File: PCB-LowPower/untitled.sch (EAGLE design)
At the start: 23 parts, among them J1 RJ45-8N-B, J2 22-27-2041-04, U1 ESP32-DEVKITC-32D, X1 MSTBA2

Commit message: revisi PCB
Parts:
- added J3: 22-27-2051-05, con-molex:22-27-2051-05
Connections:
- net 3V3: now also J3-5.S
- net GND: now also J3-1.S
- net P2_1: now also J3-4.S; no longer U1.IO5
- net P2_2: now also J3-3.S; no longer U1.IO2
- net RST_Z: now also J3-2.S
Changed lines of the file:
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@@
 <part name="R6" library="adafruit" library_urn="urn:adsk.eagle:library:420" deviceset="R-US_" device="M0805" package3d_urn="urn:adsk.eagle:package:6240587/1"/>
 <part name="GND9" library="supply1" library_urn="urn:adsk.eagle:library:371" deviceset="GND" device=""/>
+<part name="J3" library="con-molex" library_urn="urn:adsk.eagle:library:165" deviceset="22-?-05" device="27-2051" package3d_urn="urn:adsk.eagle:package:8078651/1"/>
+<part name="GND10" library="supply1" library_urn="urn:adsk.eagle:library:371" deviceset="GND" device=""/>
 </parts>
 <sheets>
@@
 <attribute name="VALUE" x="27.94" y="-25.4" size="1.778" layer="96"/>
 </instance>
+<instance part="J3" gate="-1" x="-58.42" y="-38.1" smashed="yes" rot="R180">
+<attribute name="NAME" x="-60.96" y="-37.338" size="1.524" layer="95" rot="R180"/>
+<attribute name="VALUE" x="-57.658" y="-39.497" size="1.778" layer="96" rot="R180"/>
+</instance>
+<instance part="J3" gate="-2" x="-58.42" y="-33.02" smashed="yes" rot="R180">
+<attribute name="NAME" x="-60.96" y="-32.258" size="1.524" layer="95" rot="R180"/>
+</instance>
+<instance part="J3" gate="-3" x="-58.42" y="-27.94" smashed="yes" rot="R180">
+<attribute name="NAME" x="-60.96" y="-27.178" size="1.524" layer="95" rot="R180"/>
+</instance>
+<instance part="J3" gate="-4" x="-58.42" y="-22.86" smashed="yes" rot="R180">
+<attribute name="NAME" x="-60.96" y="-22.098" size="1.524" layer="95" rot="R180"/>
+</instance>
+<instance part="J3" gate="-5" x="-58.42" y="-17.78" smashed="yes" rot="R180">
+<attribute name="NAME" x="-60.96" y="-17.018" size="1.524" layer="95" rot="R180"/>
+</instance>
+<instance part="GND10" gate="1" x="-53.34" y="-43.18" smashed="yes">
+<attribute name="VALUE" x="-55.88" y="-45.72" size="1.778" layer="96"/>
+</instance>
 </instances>
 <busses>
@@
 <wire x1="50.8" y1="-2.54" x2="50.8" y2="0" width="0.1524" layer="91"/>
 <label x="50.8" y="0" size="0.6096" layer="95" rot="R90" xref="yes"/>
+</segment>
+<segment>
+<pinref part="J3" gate="-5" pin="S"/>
+<wire x1="-55.88" y1="-17.78" x2="-53.34" y2="-17.78" width="0.1524" layer="91"/>
+<label x="-53.34" y="-17.78" size="0.6096" layer="95" xref="yes"/>
 </segment>
 </net>
@@
 <junction x="35.56" y="-17.78"/>
 </segment>
+<segment>
+<pinref part="J3" gate="-1" pin="S"/>
+<wire x1="-55.88" y1="-38.1" x2="-53.34" y2="-38.1" width="0.1524" layer="91"/>
+<pinref part="GND10" gate="1" pin="GND"/>
+<wire x1="-53.34" y1="-38.1" x2="-53.34" y2="-40.64" width="0.1524" layer="91"/>
+</segment>
 </net>
 <net name="MOSI_HSPI" class="0">
@@
 <label x="53.34" y="-15.24" size="0.6096" layer="95" xref="yes"/>
 </segment>
+<segment>
+<pinref part="J3" gate="-2" pin="S"/>
+<wire x1="-55.88" y1="-33.02" x2="-53.34" y2="-33.02" width="0.1524" layer="91"/>
+<label x="-53.34" y="-33.02" size="0.6096" layer="95" xref="yes"/>
+</segment>
 </net>
 <net name="RX_Z" class="0">
@@
 <net name="P2_1" class="0">
 <segment>
-<pinref part="U1" gate="G$1" pin="IO5"/>
-<wire x1="-5.08" y1="48.26" x2="-2.54" y2="48.26" width="0.1524" layer="91"/>
-<label x="-2.54" y="48.26" size="0.6096" layer="95" xref="yes"/>
-</segment>
-<segment>
 <pinref part="U$1" gate="G$1" pin="P2.1"/>
 <wire x1="-43.18" y1="-7.62" x2="-45.72" y2="-7.62" width="0.1524" layer="91"/>
 <label x="-45.72" y="-7.62" size="0.6096" layer="95" rot="R180" xref="yes"/>
 </segment>
+<segment>
+<pinref part="J3" gate="-4" pin="S"/>
+<wire x1="-55.88" y1="-22.86" x2="-53.34" y2="-22.86" width="0.1524" layer="91"/>
+<label x="-53.34" y="-22.86" size="0.6096" layer="95" xref="yes"/>
+</segment>
 </net>
 <net name="P2_2" class="0">
-<segment>
-<pinref part="U1" gate="G$1" pin="IO2"/>
-<wire x1="-5.08" y1="35.56" x2="-2.54" y2="35.56" width="0.1524" layer="91"/>
-<label x="-2.54" y="35.56" size="0.6096" layer="95" xref="yes"/>
-</segment>
 <segment>
 <pinref part="U$1" gate="G$1" pin="P2.2"/>
@@
 <label x="-45.72" y="-5.08" size="0.6096" layer="95" rot="R180" xref="yes"/>
 </segment>
-</net>
+<segment>
+<pinref part="J3" gate="-3" pin="S"/>
+<wire x1="-55.88" y1="-27.94" x2="-53.34" y2="-27.94" width="0.1524" layer="91"/>
+<label x="-53.34" y="-27.94" size="0.6096" layer="95" xref="yes"/>
+</segment>
+</net>

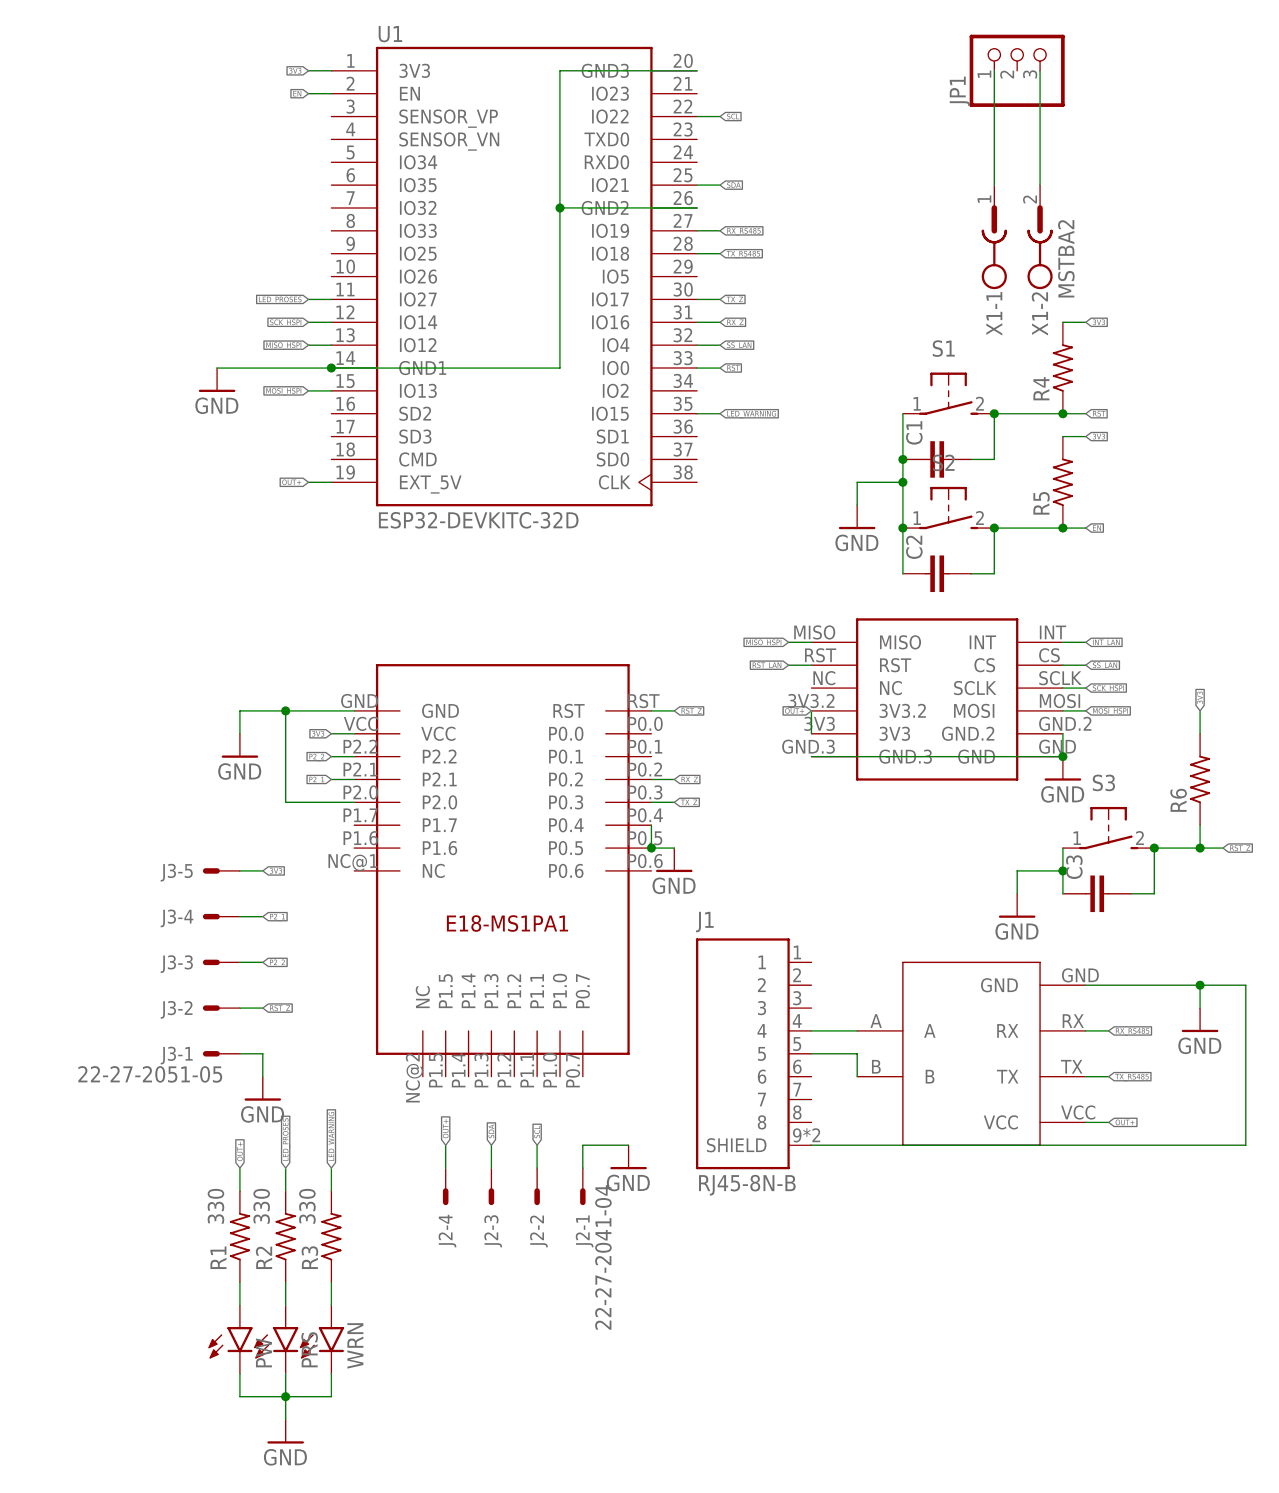
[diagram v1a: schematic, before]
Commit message: menambahkan rangkaian PCB TOP
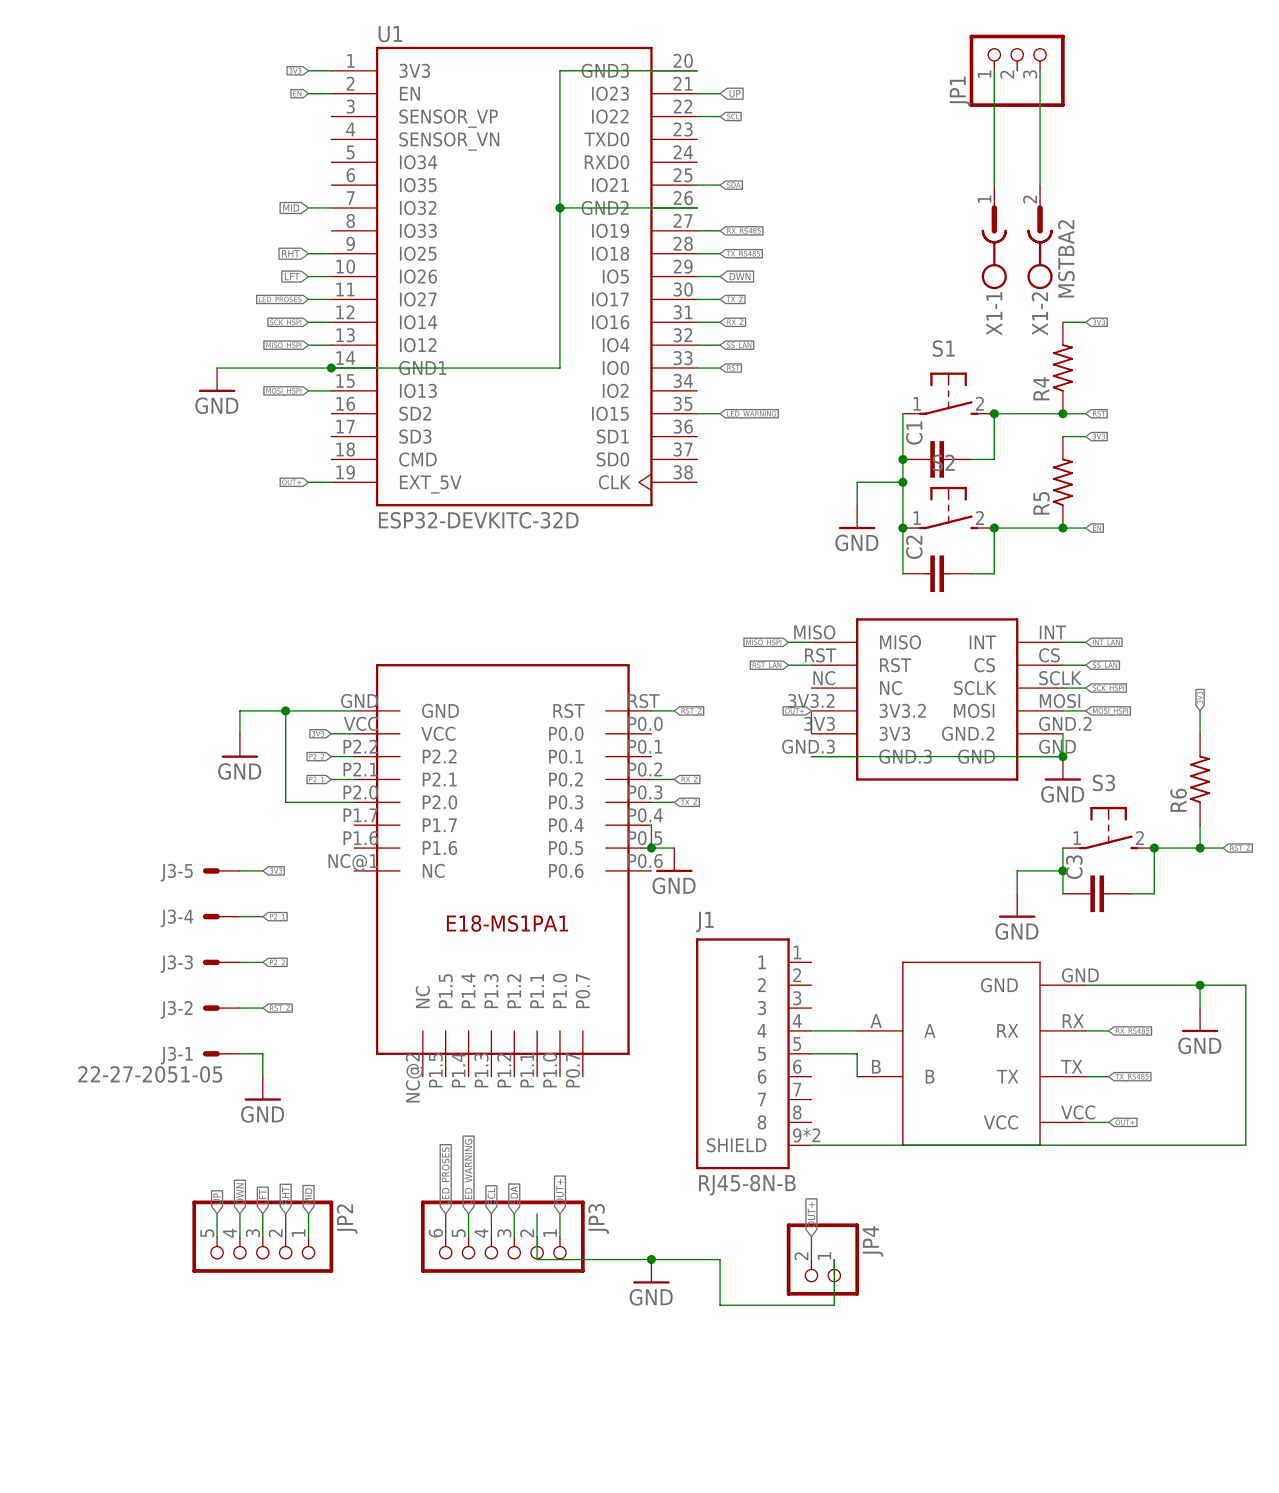
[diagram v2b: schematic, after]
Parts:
- removed J2: 22-27-2041-04, con-molex:22-27-2041-04
- removed PRS, PW, WRN: TLLR4400, led:TLLR4400
- removed R1, R2, R3: 330, adafruit:R-US_M0805
- added JP2: (no value), pinhead:PINHD-1X5
- added JP3: (no value), pinhead:PINHD-1X6
- added JP4: (no value), pinhead:PINHD-1X2
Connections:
- removed net N$4: PW.A, R1.1
- removed net N$5: PRS.A, R2.1
- removed net N$6: R3.1, WRN.A
- new net DWN: JP2.4, U1.IO5
- new net LFT: JP2.3, U1.IO26
- new net MID: JP2.1, U1.IO32
- new net RHT: JP2.2, U1.IO25
- new net UP: JP2.5, U1.IO23
- net GND: now also JP3.2, JP4.1; no longer J2-1.S, PRS.C, PW.C, WRN.C
- net LED_PROSES: now also JP3.6; no longer R2.2
- net LED_WARNING: now also JP3.5; no longer R3.2
- net OUT+: now also JP3.1, JP4.2; no longer J2-4.S, R1.2
- net SCL: now also JP3.4; no longer J2-2.S
- net SDA: now also JP3.3; no longer J2-3.S
